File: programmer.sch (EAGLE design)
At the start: 20 parts, among them U1 ATMEGA8U2AU, X1 16MHz

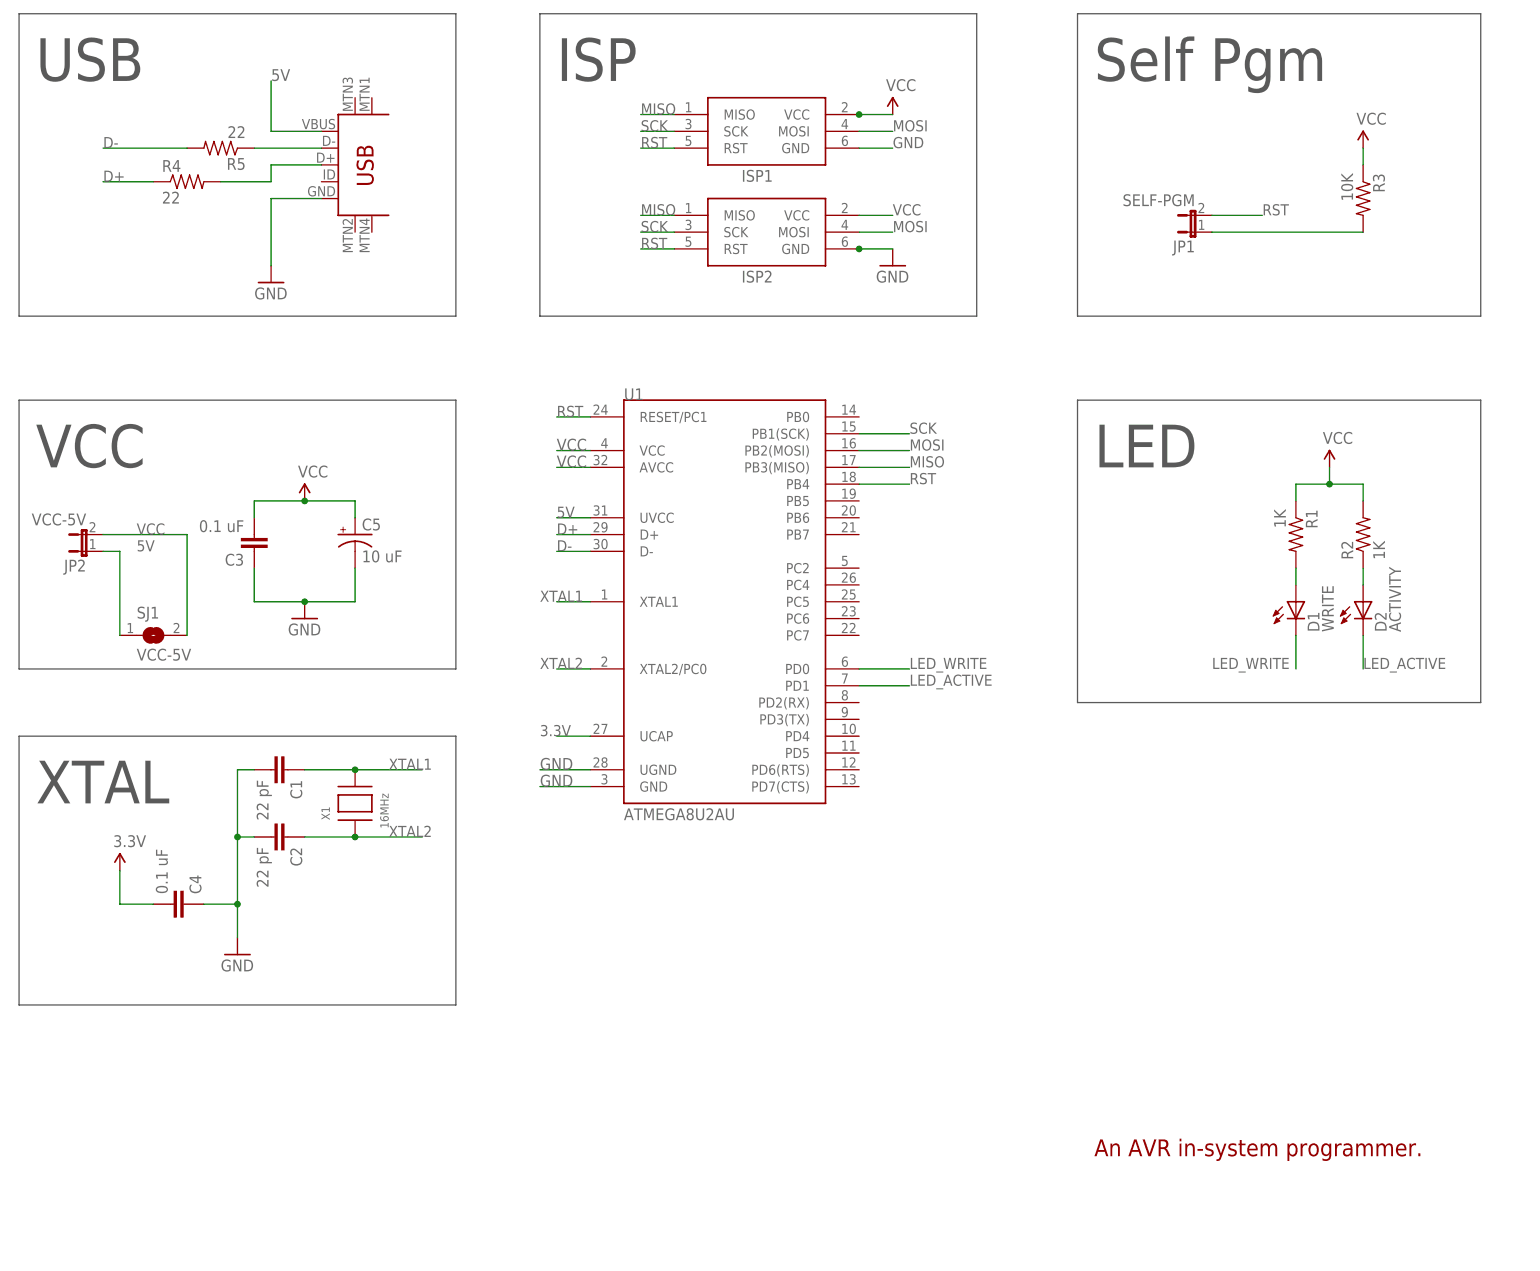
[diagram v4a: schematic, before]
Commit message: Fixed error in self-program jumper. Balanced components.
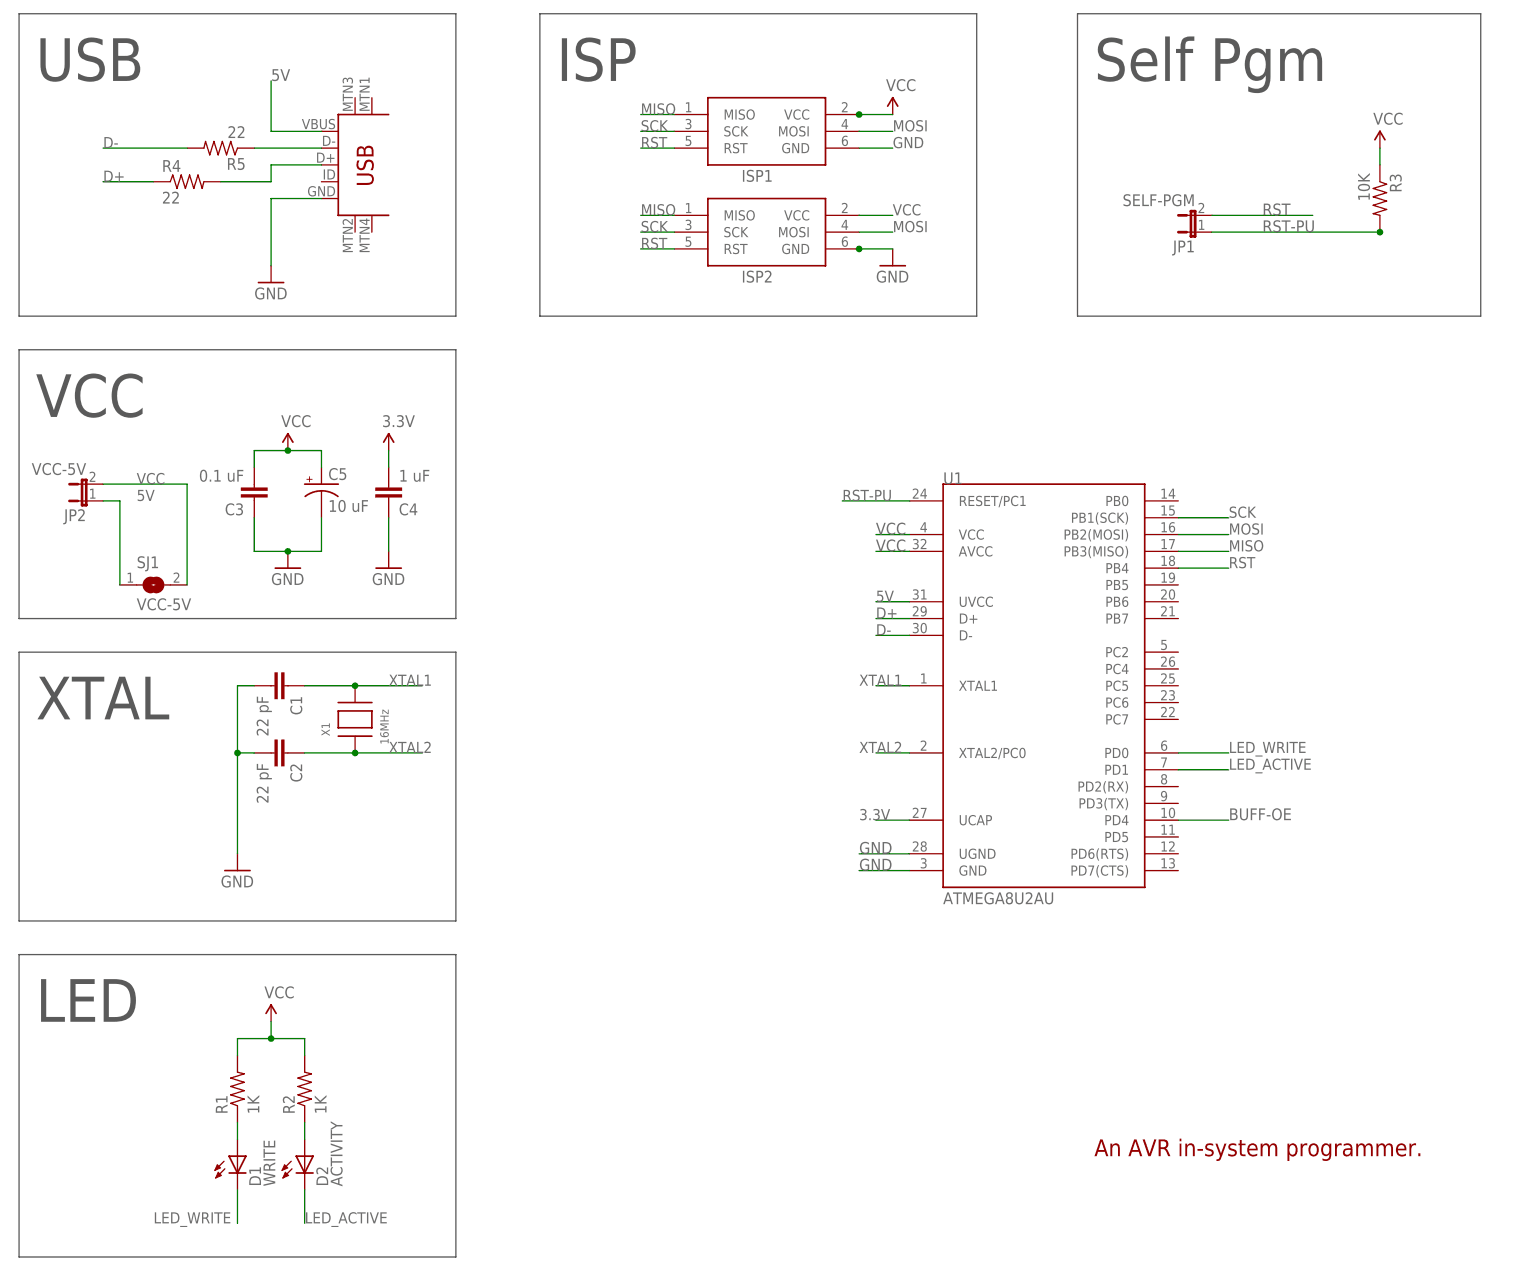
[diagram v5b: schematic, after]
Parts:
- C4: value 0.1 uF -> 1 uF
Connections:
- removed net RST_JP1: JP1.1, R3.2
- new net BUFF-OE: U1.PD4
- new net RST-PU: JP1.1, R3.2, U1.RESET/PC1
- net N$3: now also R1.1; no longer R1.2
- net RST: no longer U1.RESET/PC1
- net VCC: now also R1.2; no longer R1.1
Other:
- moved on the sheet: C1, C2, C3, C4, C5, D1, D2, JP2, R1, R2, R3, SJ1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

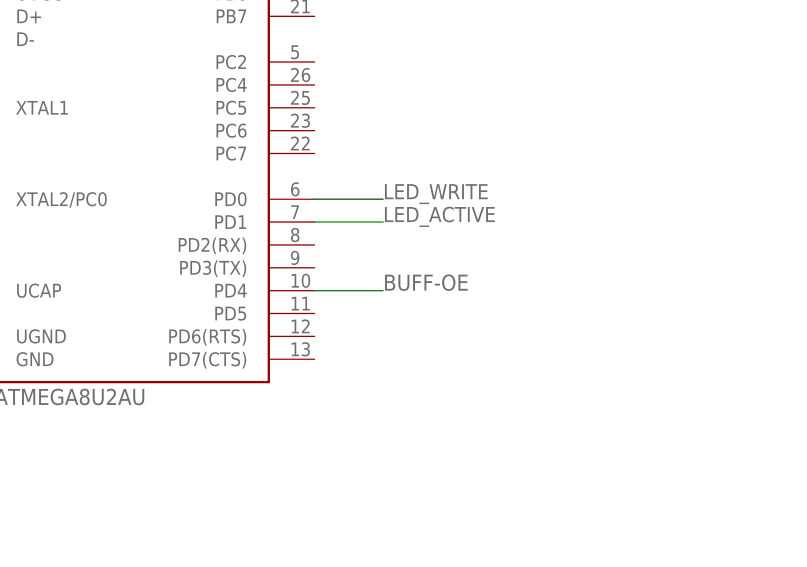
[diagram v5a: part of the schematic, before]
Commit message: Removed BUFF-OE.
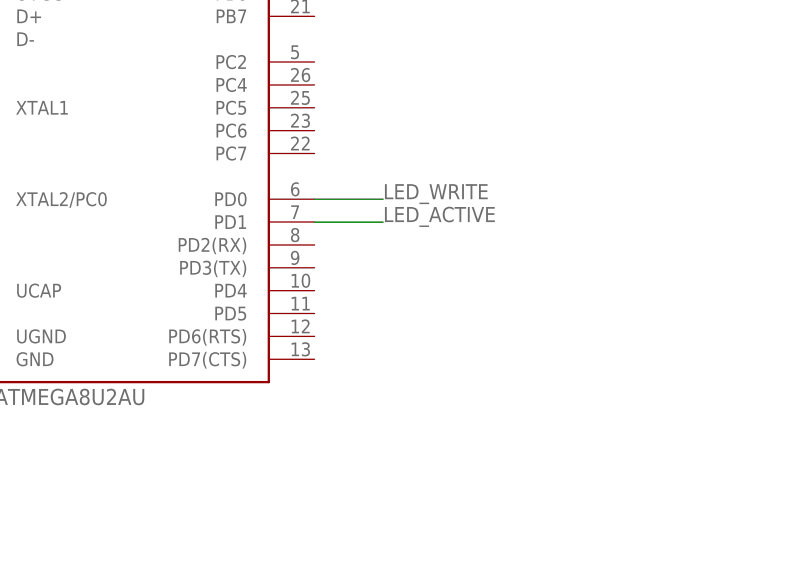
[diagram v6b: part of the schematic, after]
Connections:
- removed net BUFF-OE: U1.PD4
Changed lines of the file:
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@@
-</segment>
-</net>
-<net name="BUFF-OE" class="0">
-<segment>
-<pinref part="U1" gate="G$1" pin="PD4"/>
-<wire x1="114.3" y1="17.78" x2="121.92" y2="17.78" width="0.1524" layer="91"/>
-<label x="121.92" y="17.78" size="1.778" layer="95" font="vector"/>
 </segment>
 </net>

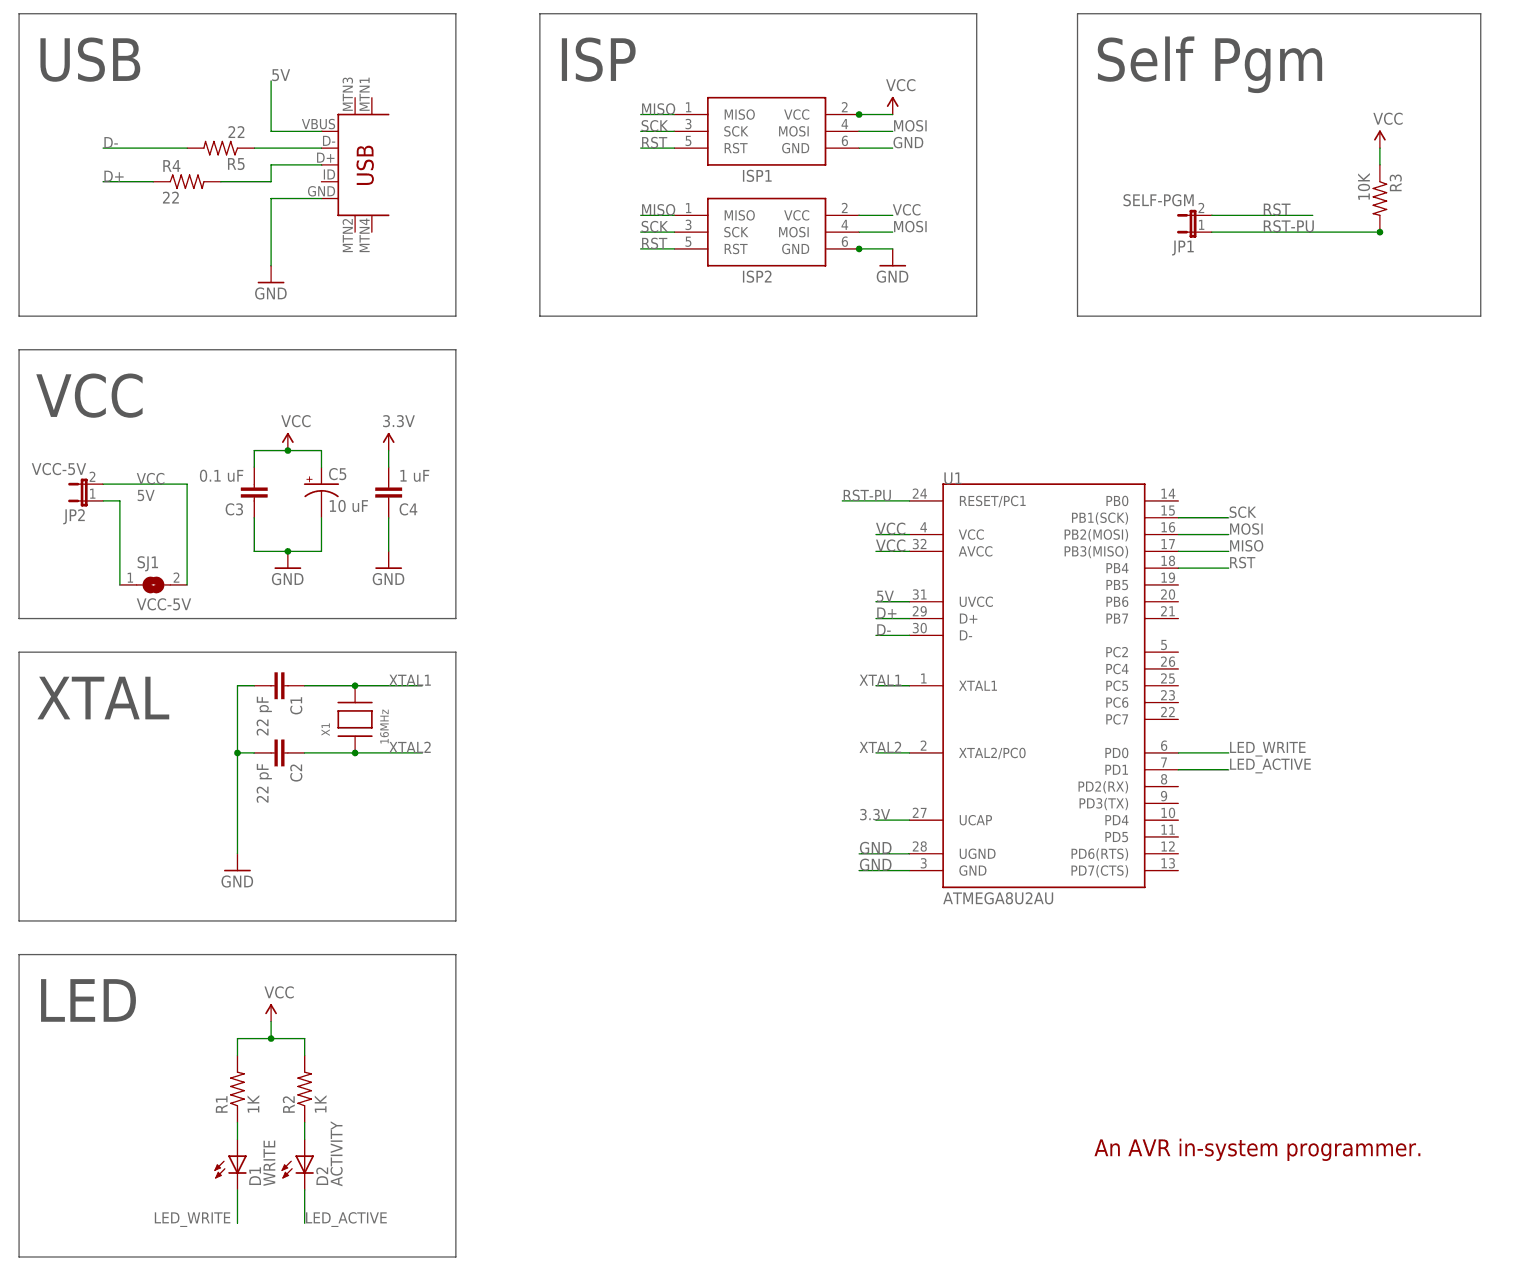
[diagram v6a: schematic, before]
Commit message: Added buffer and JTAG/voltage pinouts.
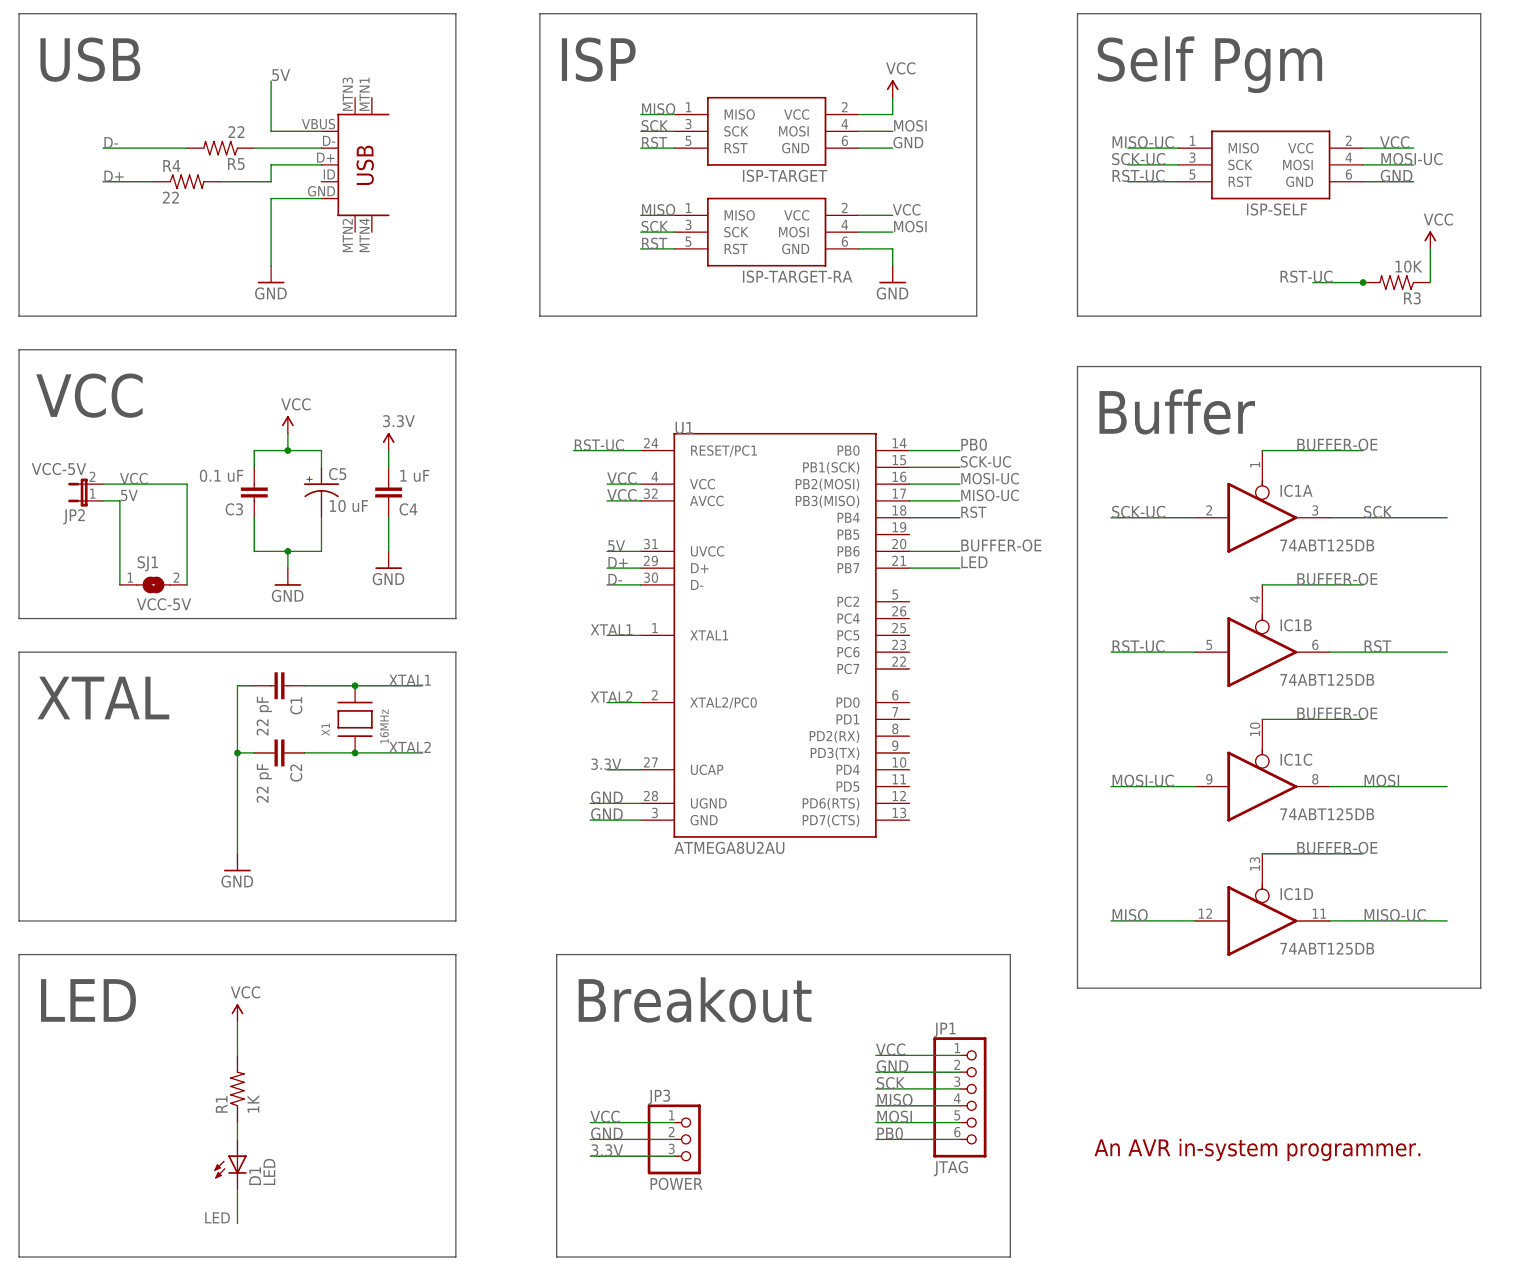
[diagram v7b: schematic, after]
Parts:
- removed D2: ACTIVITY, adafruit:LEDSMT1206
- removed R2: 1K, SparkFun:RESISTOR0805-RES
- added IC1: 74ABT125DB, 74xx-us:74ABT125DB
- added ISP-SELF: AVRISP-6, adafruit:AVRISP-6
- added JP3: POWER, adafruit:PINHD-1X3
- D1: value WRITE -> LED
- JP1: value SELF-PGM -> JTAG; device SparkFun:JUMPER-2PTH -> adafruit:PINHD-1X6
- renumbered ISP1 to ISP-TARGET, ISP2 to ISP-TARGET-RA
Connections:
- removed net LED_ACTIVE: D2.C, U1.PD1
- removed net LED_WRITE: D1.C, U1.PD0
- removed net N$1: D2.A, R2.1
- removed net RST-PU: JP1.1, R3.2, U1.RESET/PC1
- new net BUFFER-OE: IC1A.OE, IC1B.OE, IC1C.OE, IC1D.OE, U1.PB6
- new net LED: D1.C, U1.PB7
- new net MISO-UC: IC1D.O, ISP-SELF.MISO, U1.PB3(MISO)
- new net MOSI-UC: IC1C.I, ISP-SELF.MOSI, U1.PB2(MOSI)
- new net PB0: JP1.6, U1.PB0
- new net RST-UC: IC1B.I, ISP-SELF.RST, R3.2, U1.RESET/PC1
- new net SCK-UC: IC1A.I, ISP-SELF.SCK, U1.PB1(SCK)
- net 3.3V: now also JP3.3
- net GND: now also ISP-SELF.GND, JP1.2, JP3.2
- net MISO: now also IC1D.I, JP1.4; no longer U1.PB3(MISO)
- net MOSI: now also IC1C.O, JP1.5; no longer U1.PB2(MOSI)
- net RST: now also IC1B.O; no longer JP1.2
- net SCK: now also IC1A.O, JP1.3; no longer U1.PB1(SCK)
- net VCC: now also ISP-SELF.VCC, JP1.1, JP3.1; no longer R2.2
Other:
- note added: "Breakout"
- note added: "Buffer"
- moved on the sheet: R3, U1

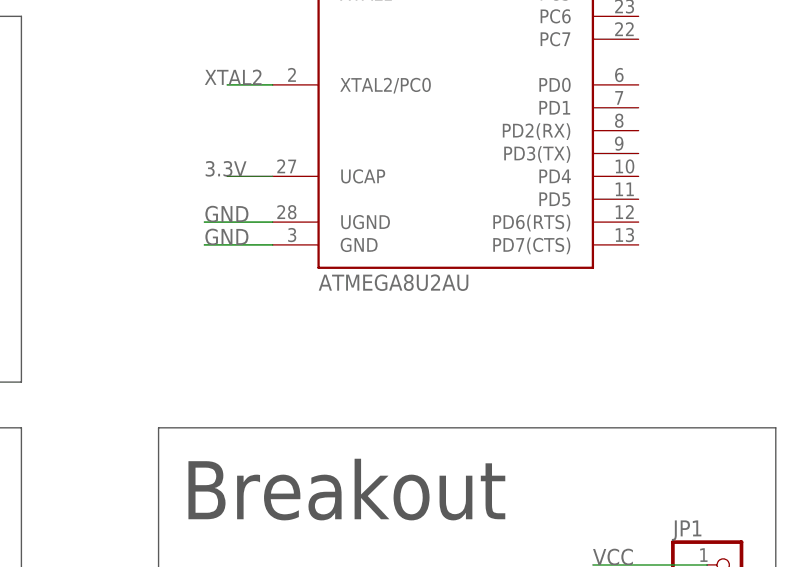
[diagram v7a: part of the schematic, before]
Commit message: Fixed '125 name on board.
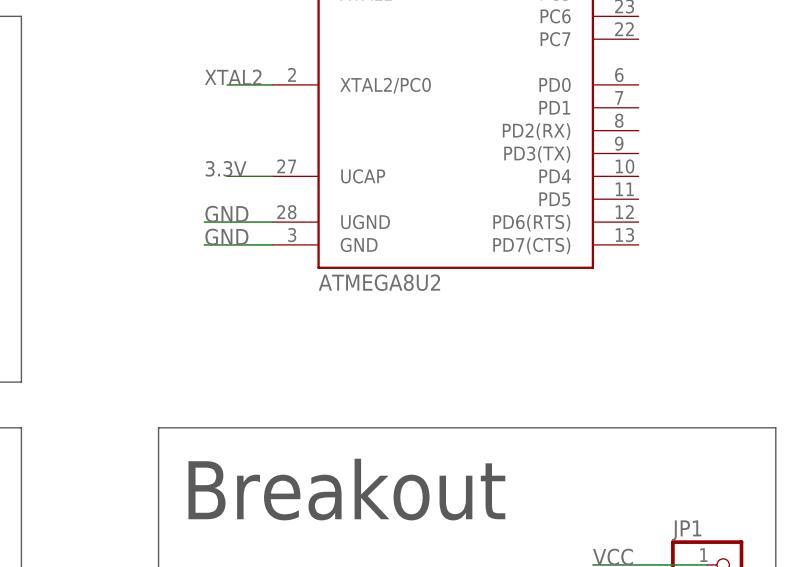
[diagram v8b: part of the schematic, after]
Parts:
- U1: value ATMEGA8U2AU -> ATMEGA8U2
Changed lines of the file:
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@@
 </classes>
 <parts>
-<part name="U1" library="SparkFun" deviceset="ATMEGA8U2" device="AU"/>
+<part name="U1" library="SparkFun" deviceset="ATMEGA8U2" device="AU" value="ATMEGA8U2"/>
 <part name="USB" library="SparkFun" deviceset="USB-MINIB" device="-5PIN"/>
 <part name="C1" library="SparkFun" deviceset="CAP" device="0805" value="22 pF"/>
